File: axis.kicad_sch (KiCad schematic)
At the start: 47 parts, among them J101 CORTEX-DEBUG, J102 JAE_DX07S016JA3, SW101 SW_Push, SW102 SW_Push, U101 BHI160, U102 ATSAMD51G, U103 BMM150, U104 AP2112K-3.3, Y101 32k768

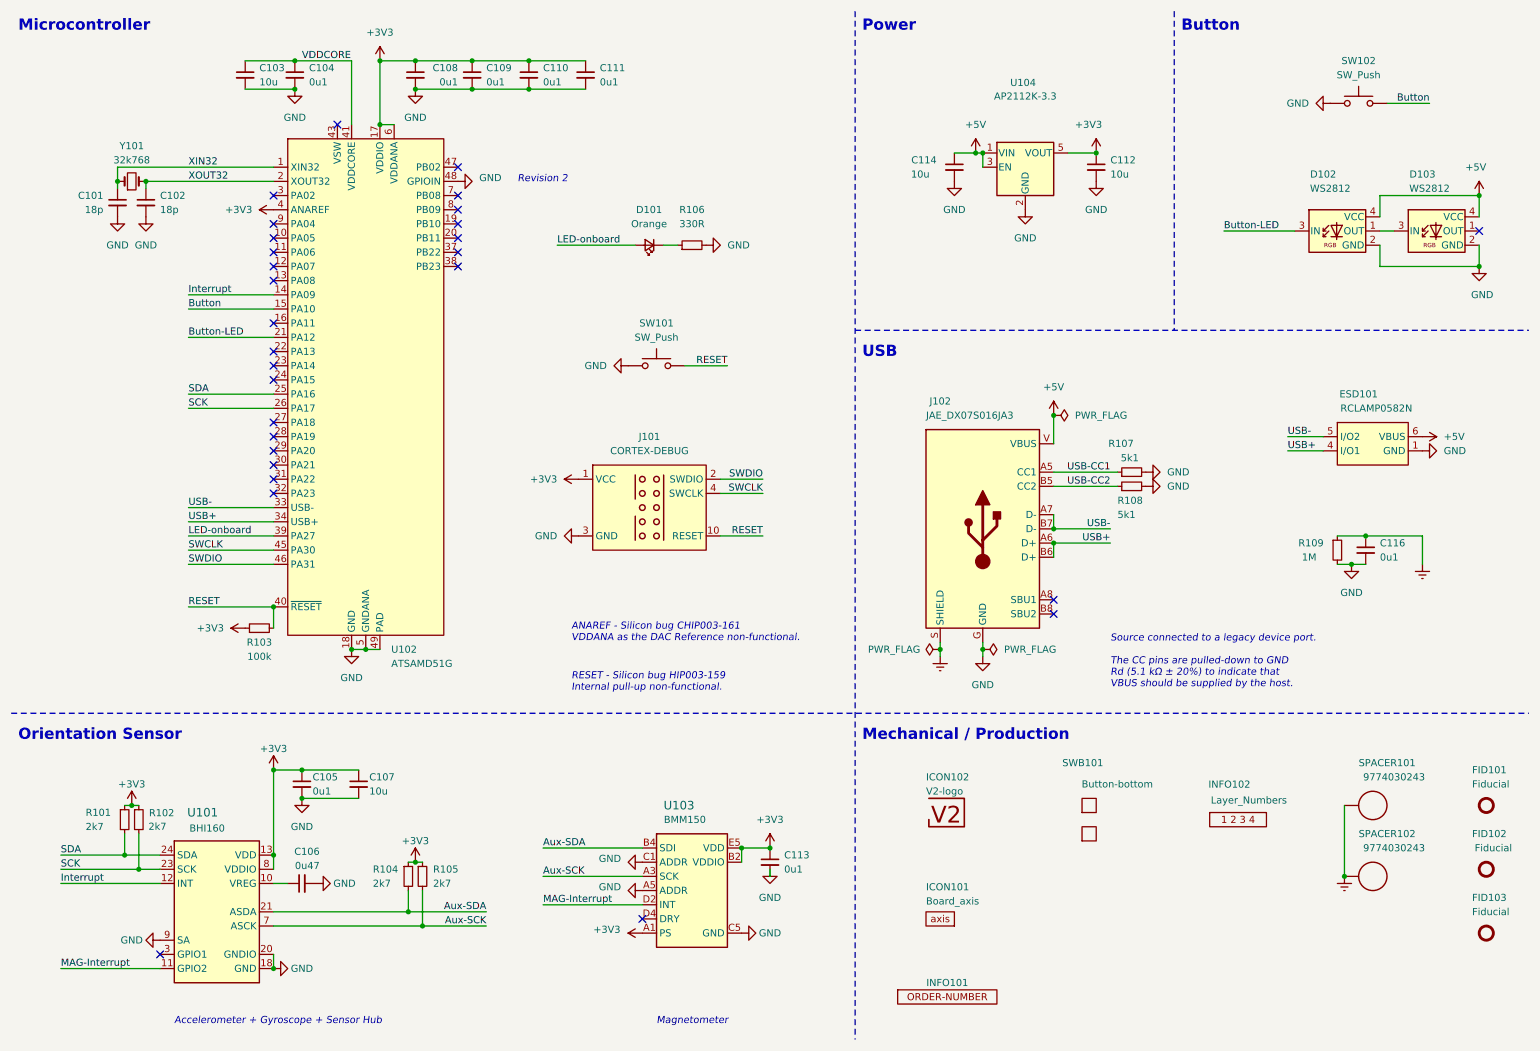
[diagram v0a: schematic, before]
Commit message: Replace LDO
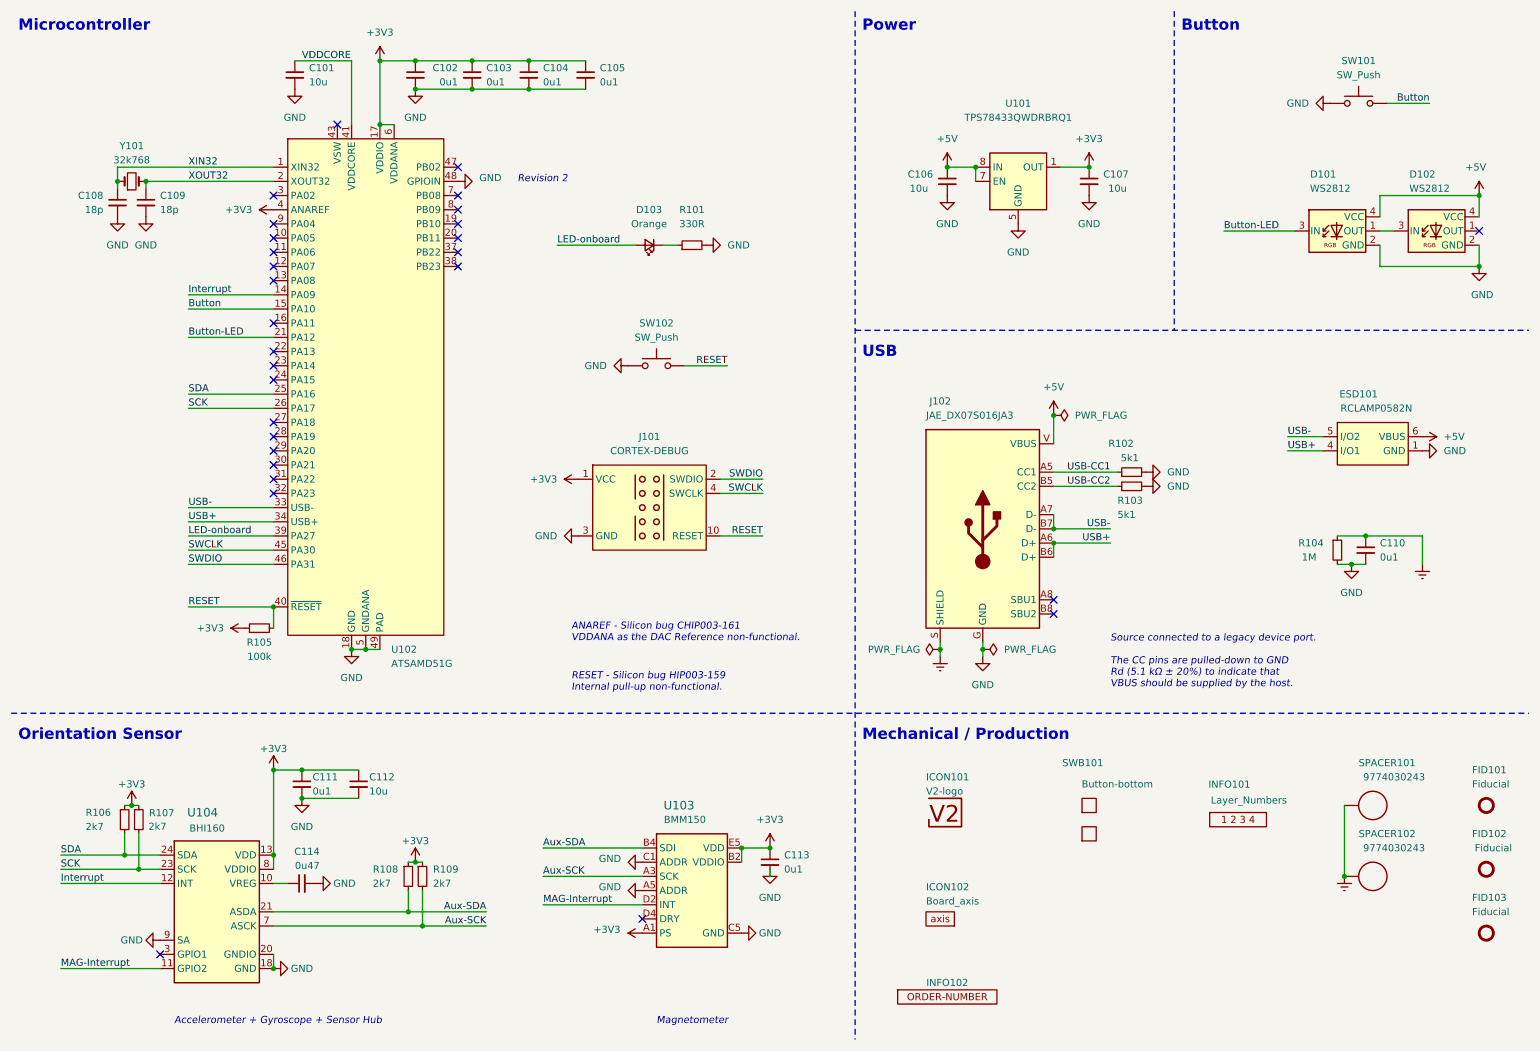
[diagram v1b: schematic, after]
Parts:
- removed C104: 0u1, Capacitor_SMD:C_0603_1608Metric, symbol Device:C_Small
- removed C114: 10u, Capacitor_SMD:C_0603_1608Metric, symbol Device:C_Small
- removed U104: AP2112K-3.3, Package_TO_SOT_SMD:SOT-23-5, symbol Regulator_Linear:AP2112K-3.3
- added C106: 10u, Capacitor_SMD:C_0603_1608Metric, symbol Device:C_Small
- added U101: TPS78433QWDRBRQ1, V2_Package_SON:VSON-8-1_3x3mm_P0.65_EP1.65x2.4mm, symbol V2_Regulator_Linear:TPS78433QWDRBRQ1
- renumbered C103 to C101, C108 to C102, C109 to C103, C110 to C104, C111 to C105, C112 to C107, C101 to C108, C102 to C109, C116 to C110, C105 to C111, C107 to C112, C106 to C114, D102 to D101, D103 to D102, D101 to D103, ICON102 to ICON101, ICON101 to ICON102, INFO102 to INFO101, INFO101 to INFO102, R106 to R101, R107 to R102, R108 to R103, R109 to R104, R103 to R105, R101 to R106, R102 to R107, R104 to R108, R105 to R109, SW102 to SW101, SW101 to SW102, U101 to U104
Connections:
- net +3V3: now also U101.1 (OUT)
- net +5V: now also C106.1, U101.7 (EN), U101.8 (IN)
- net GND: now also C106.2, U101.5 (GND), U101.9 (GND)
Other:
- moved on the sheet: C101, C107
